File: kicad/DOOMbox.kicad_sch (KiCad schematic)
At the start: 1 part, among them U1 Pico

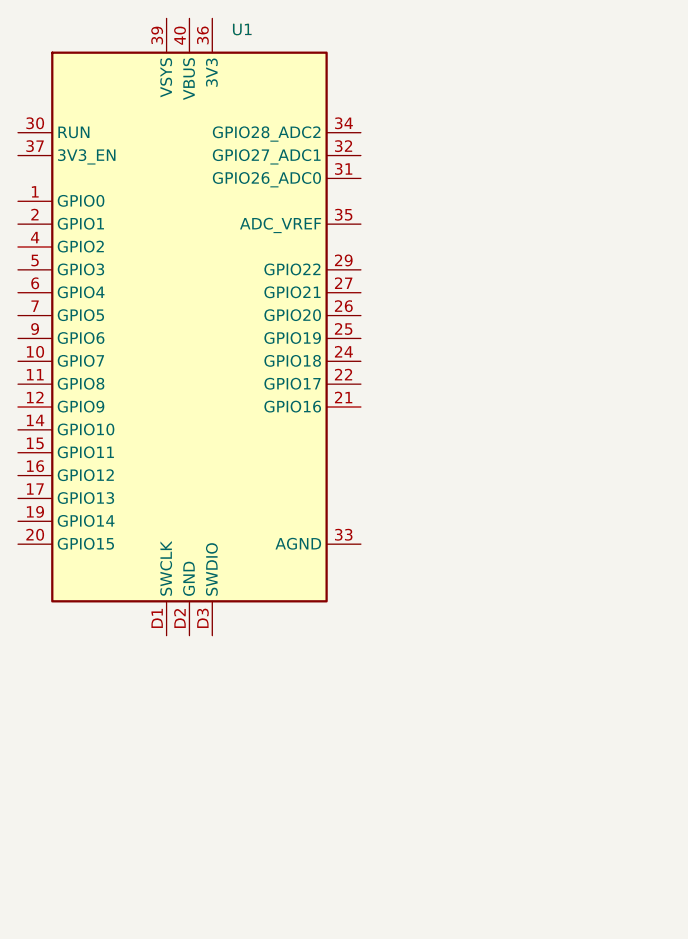
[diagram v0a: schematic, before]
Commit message: Track necessary KiCad libraries + symbols
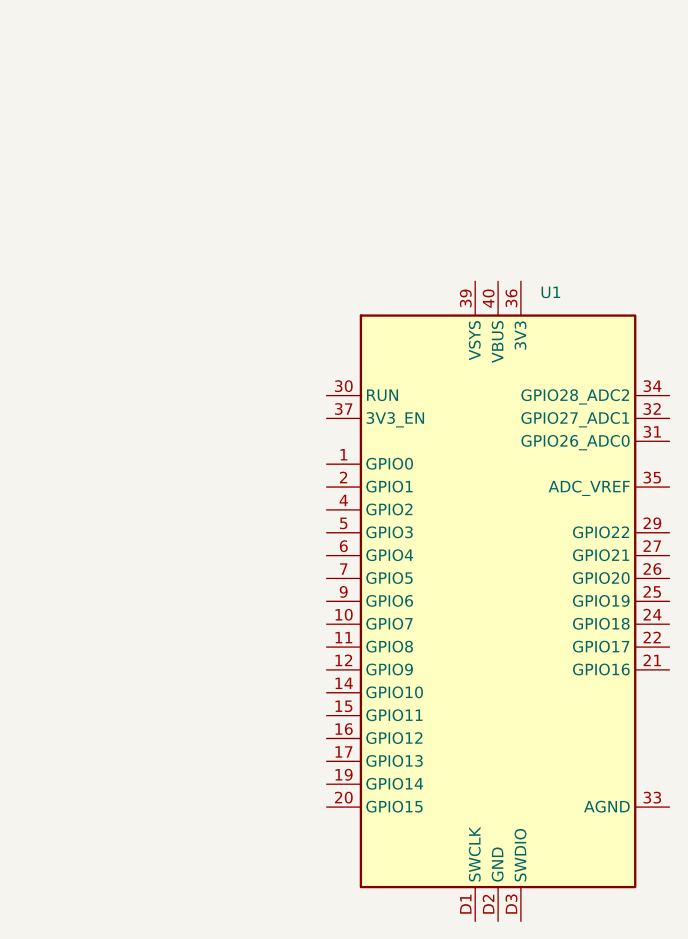
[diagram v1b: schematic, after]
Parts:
- removed U1: Pico, RPi_Pico:RPi_Pico_SMD_TH, symbol MCU_RaspberryPi_and_Boards:Pico
- added U1: RPi_Pico_SMD_TH, MCU_RPi:RPi_Pico_SMD_TH, symbol MCU_RPi:RPi_Pico_SMD_TH
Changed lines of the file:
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@@
 	(paper "A4")
 	(symbol
-		(lib_id "MCU_RaspberryPi_and_Boards:Pico")
-		(at 71.12 62.23 0)
+		(lib_id "MCU_RPi:RPi_Pico_SMD_TH")
+		(at 105.41 91.44 0)
 		(unit 1)
 		(exclude_from_sim no)
@@
 		(fields_autoplaced yes)
 		(property "Reference" "U1"
-			(at 75.8033 31.75 0)
+			(at 110.0933 60.96 0)
 			(effects
 				(font
@@
 			)
 		)
-		(property "Value" "Pico"
-			(at 71.12 72.898 0)
+		(property "Value" "RPi_Pico_SMD_TH"
+			(at 105.41 102.108 0)
 			(effects
 				(font
@@
 			)
 		)
-		(property "Footprint" "RPi_Pico:RPi_Pico_SMD_TH"
-			(at 70.612 70.358 0)
+		(property "Footprint" "MCU_RPi:RPi_Pico_SMD_TH"
+			(at 104.902 99.568 0)
 			(effects
 				(font
@@
 		)
 		(property "Datasheet" ""
-			(at 71.12 62.23 0)
+			(at 105.41 91.44 0)
 			(effects
 				(font
@@
 		)
 		(property "Description" ""
-			(at 71.12 62.23 0)
+			(at 105.41 91.44 0)
 			(effects
 				(font
@@
 			)
 		)
-		(pin "34"
+		(pin "D2"
+		)
+		(pin "D1"
+		)
+		(pin "33"
+		)
+		(pin "29"
+		)
+		(pin "19"
+		)
+		(pin "26"
+		)
+		(pin "35"
+		)
+		(pin "7"
+		)
+		(pin "16"
+		)
+		(pin "11"
+		)
+		(pin "D3"
+		)
+		(pin "25"
+		)
+		(pin "9"
+		)
+		(pin "21"
+		)
+		(pin "31"
+		)
+		(pin "22"
+		)
+		(pin "40"
+		)
+		(pin "24"
+		)
+		(pin "10"
+		)
+		(pin "27"
+		)
+		(pin "36"
+		)
+		(pin "20"
+		)
+		(pin "39"
+		)
+		(pin "17"
 		)
 		(pin "32"
 		)
-		(pin "36"
-		)
-		(pin "26"
-		)
-		(pin "D3"
-		)
-		(pin "14"
-		)
-		(pin "39"
+		(pin "34"
 		)
 		(pin "37"
@@
 		(pin "30"
 		)
+		(pin "1"
+		)
 		(pin "5"
 		)
-		(pin "22"
+		(pin "4"
 		)
-		(pin "D2"
+		(pin "2"
 		)
-		(pin "24"
+		(pin "12"
 		)
-		(pin "29"
-		)
-		(pin "7"
-		)
-		(pin "40"
-		)
-		(pin "35"
-		)
-		(pin "19"
+		(pin "14"
 		)
 		(pin "15"
 		)
-		(pin "9"
-		)
-		(pin "17"
-		)
-		(pin "4"
-		)
-		(pin "16"
-		)
-		(pin "25"
-		)
-		(pin "10"
-		)
-		(pin "D1"
-		)
 		(pin "6"
 		)
-		(pin "12"
-		)
-		(pin "31"
-		)
-		(pin "20"
-		)
-		(pin "33"
-		)
-		(pin "2"
-		)
-		(pin "21"
-		)
-		(pin "27"
-		)
-		(pin "11"
-		)
-		(pin "1"
-		)
 		(instances

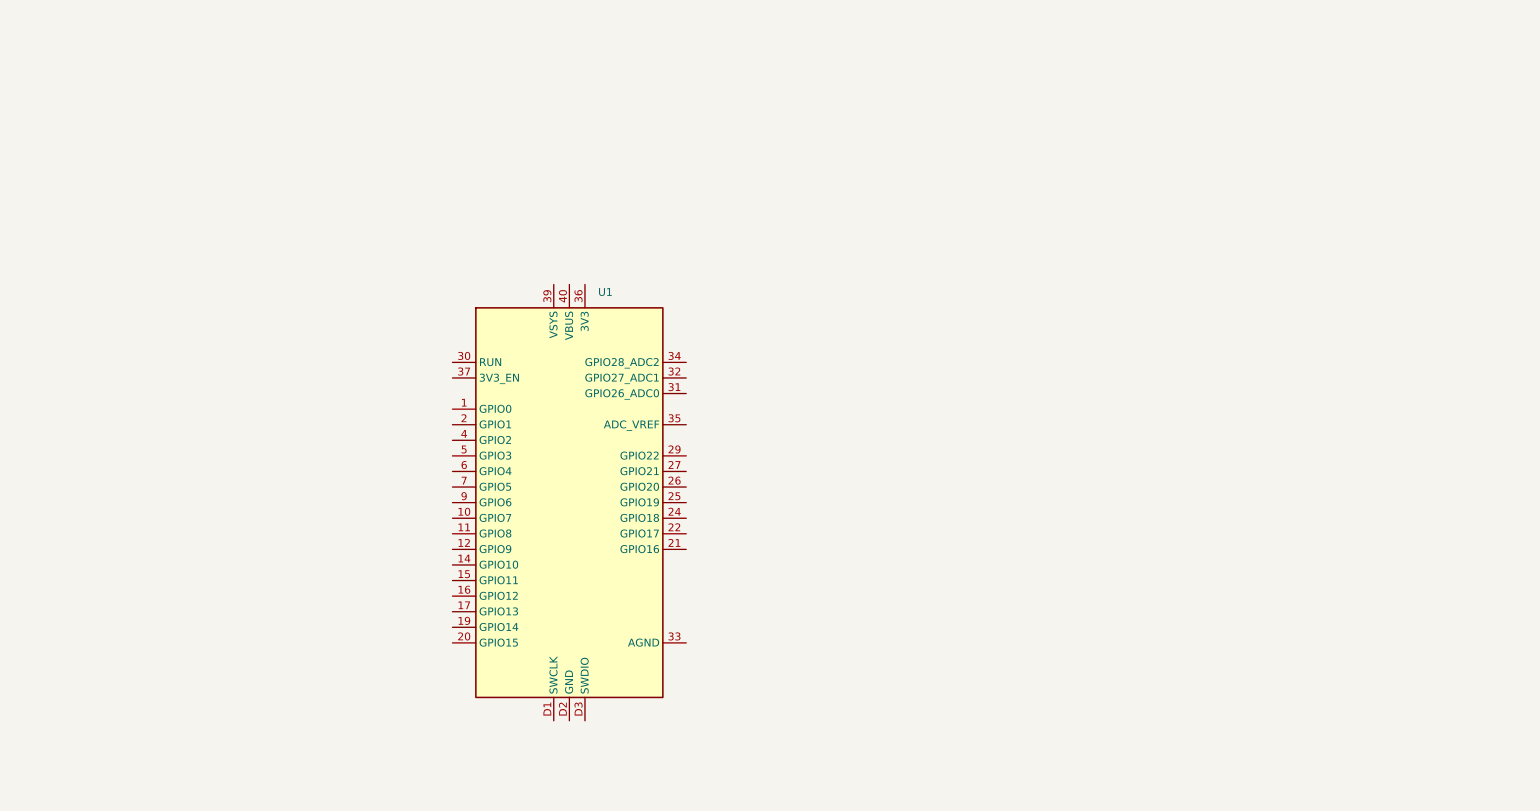
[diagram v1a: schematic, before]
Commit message: Schematic: add resistor ladder DACs for video data output
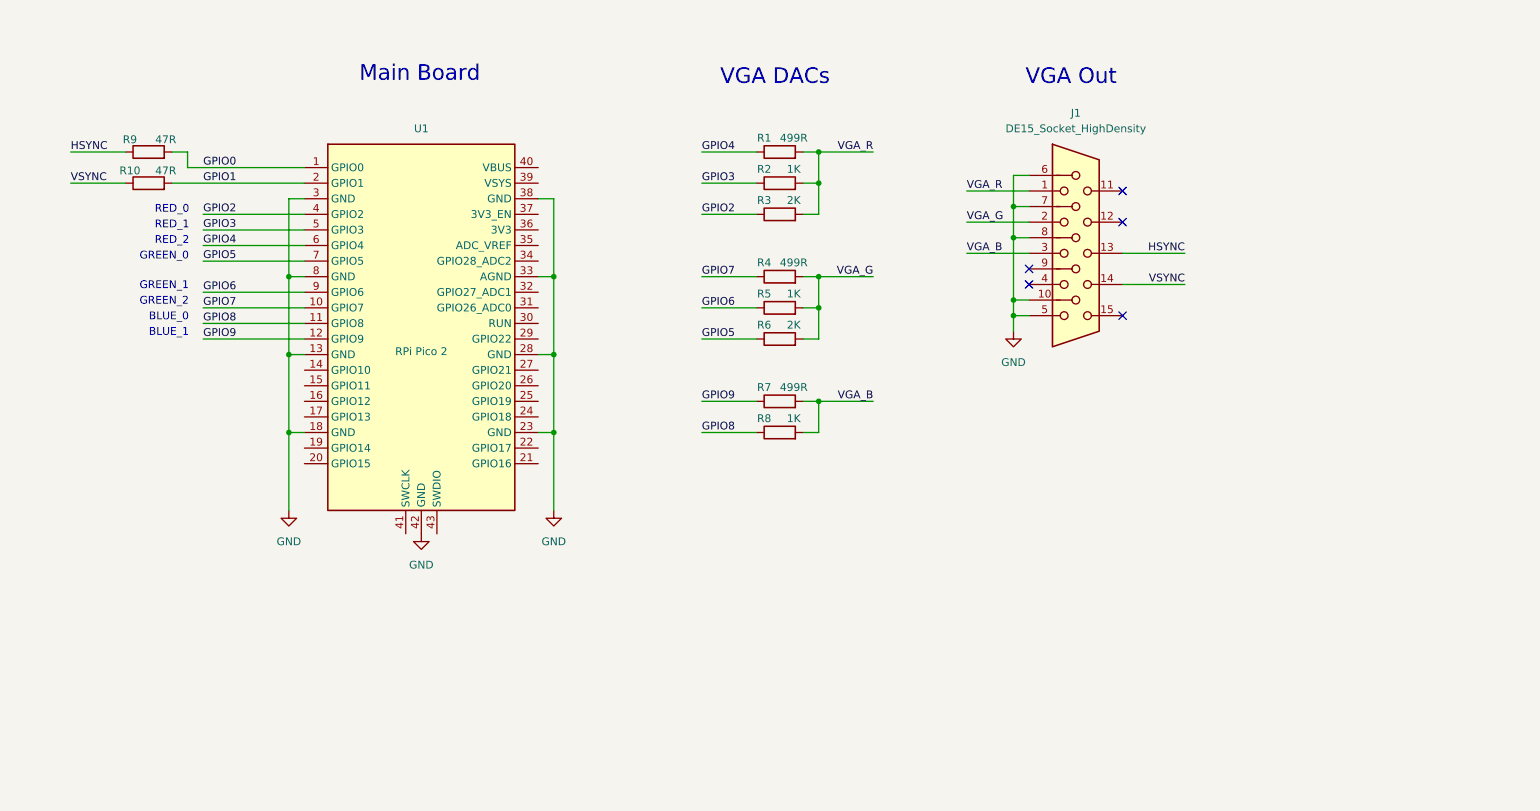
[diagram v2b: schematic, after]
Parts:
- added J1: DE15_Socket_HighDensity, symbol Connector:DE15_Socket_HighDensity
- added R1, R4, R7: 499R, symbol Device:R
- added R10, R9: 47R, symbol Device:R
- added R2, R5, R8: 1K, symbol Device:R
- added R3, R6: 2K, symbol Device:R
- U1: value RPi_Pico_SMD_TH -> RPi Pico 2
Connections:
- net GPIO0: now reaches U1.1 (GPIO0)
- net GPIO0: now also R9.2
- net GPIO7: now reaches U1.10 (GPIO7)
- net GPIO7: now also R4.1
- net GPIO8: now reaches U1.11 (GPIO8)
- net GPIO8: now also R8.1
- net GPIO9: now reaches U1.12 (GPIO9)
- net GPIO9: now also R7.1
- net GPIO1: now reaches U1.2 (GPIO1)
- net GPIO1: now also R10.2
- net GND: now reaches U1.33 (AGND)
- net GND: now also U1.13 (GND), U1.18 (GND), U1.23 (GND), U1.28 (GND), U1.3 (GND), U1.38 (GND), U1.42 (GND), U1.8 (GND), J1.10, J1.5, J1.6, J1.7, J1.8
- net GPIO2: now reaches U1.4 (GPIO2)
- net GPIO2: now also R3.1
- net GPIO3: now reaches U1.5 (GPIO3)
- net GPIO3: now also R2.1
- net GPIO4: now reaches U1.6 (GPIO4)
- net GPIO4: now also R1.1
- net GPIO5: now reaches U1.7 (GPIO5)
- net GPIO5: now also R6.1
- net GPIO6: now reaches U1.9 (GPIO6)
- net GPIO6: now also R5.1
- new net HSYNC: J1.13, R9.1
- new net VGA_B: J1.3, R7.2, R8.2
- new net VGA_G: J1.2, R4.2, R5.2, R6.2
- new net VGA_R: J1.1, R1.2, R2.2, R3.2
- new net VSYNC: J1.14, R10.1
- no-connect marks 0 -> 5
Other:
- note added: "BLUE_0"
- note added: "BLUE_1"
- note added: "GREEN_0"
- note added: "GREEN_1"
- note added: "GREEN_2"
- note added: "Main Board"
- note added: "RED_0"
- note added: "RED_1"
- note added: "RED_2"
- note added: "VGA DACs"
- note added: "VGA Out"

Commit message: Add component sheet + VGA output note in schematic
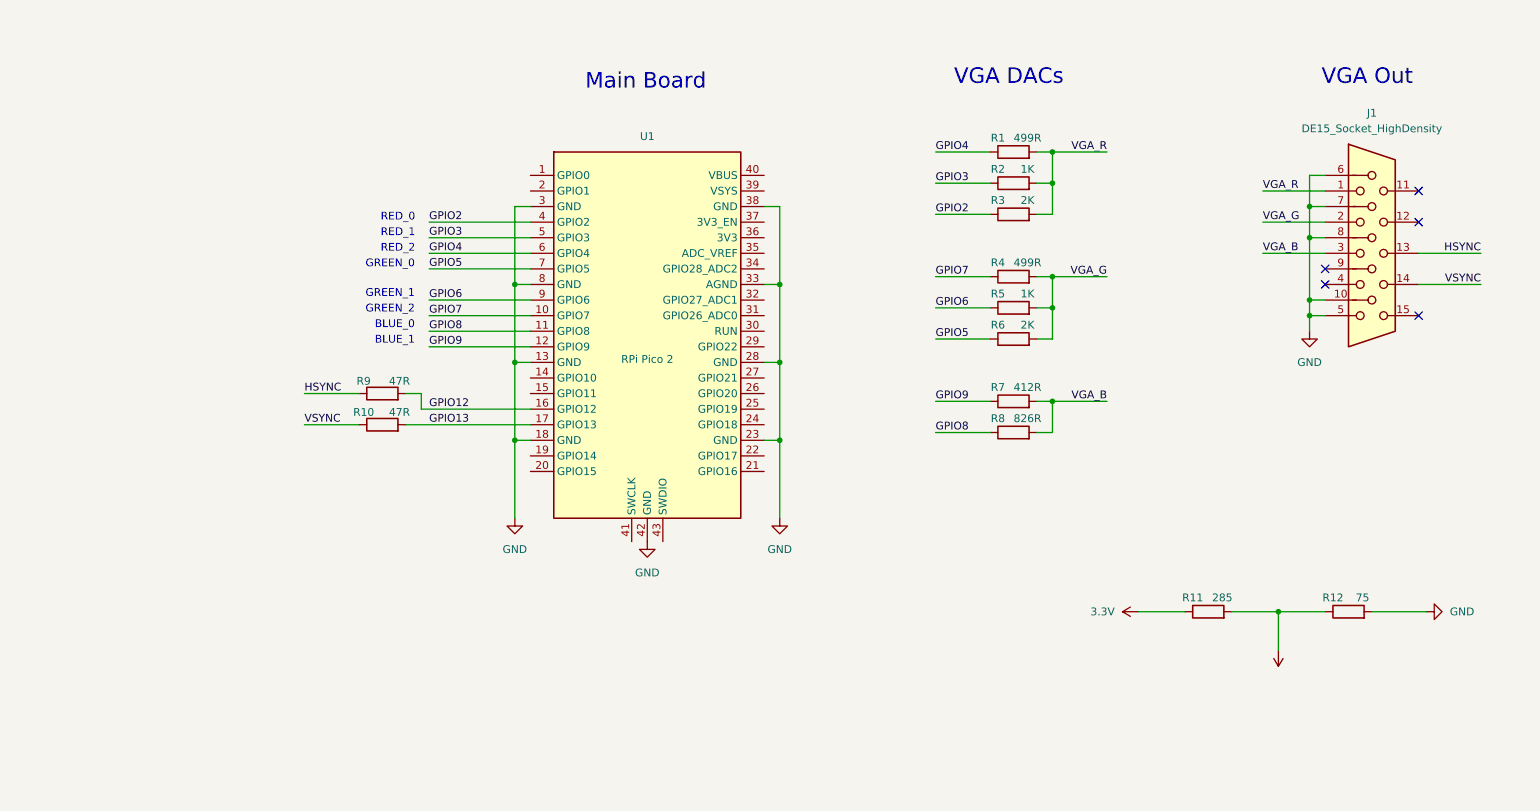
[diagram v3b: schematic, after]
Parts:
- added R11: 285, symbol Device:R
- added R12: 75, symbol Device:R
- R7: value 499R -> 412R
- R8: value 1K -> 826R
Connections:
- net GND: now also R12.2
- net GPIO12: now reaches U1.16 (GPIO12)
- net GPIO12: now also R9.2
- net GPIO13: now reaches U1.17 (GPIO13)
- net GPIO13: now also R10.2
- net GPIO0: no longer names the net of U1.1 (GPIO0)
- net GPIO0: no longer R9.2
- net GPIO1: no longer names the net of U1.2 (GPIO1)
- net GPIO1: no longer R10.2
- new net: R11.2, R12.1
- new net 3.3V: R11.1
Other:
- moved on the sheet: J1, R1, R10, R2, R3, R4, R5, R6, R7, R8, R9, U1

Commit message: Finalise VGA output schematic now w/ MCP23S08 SPI expander
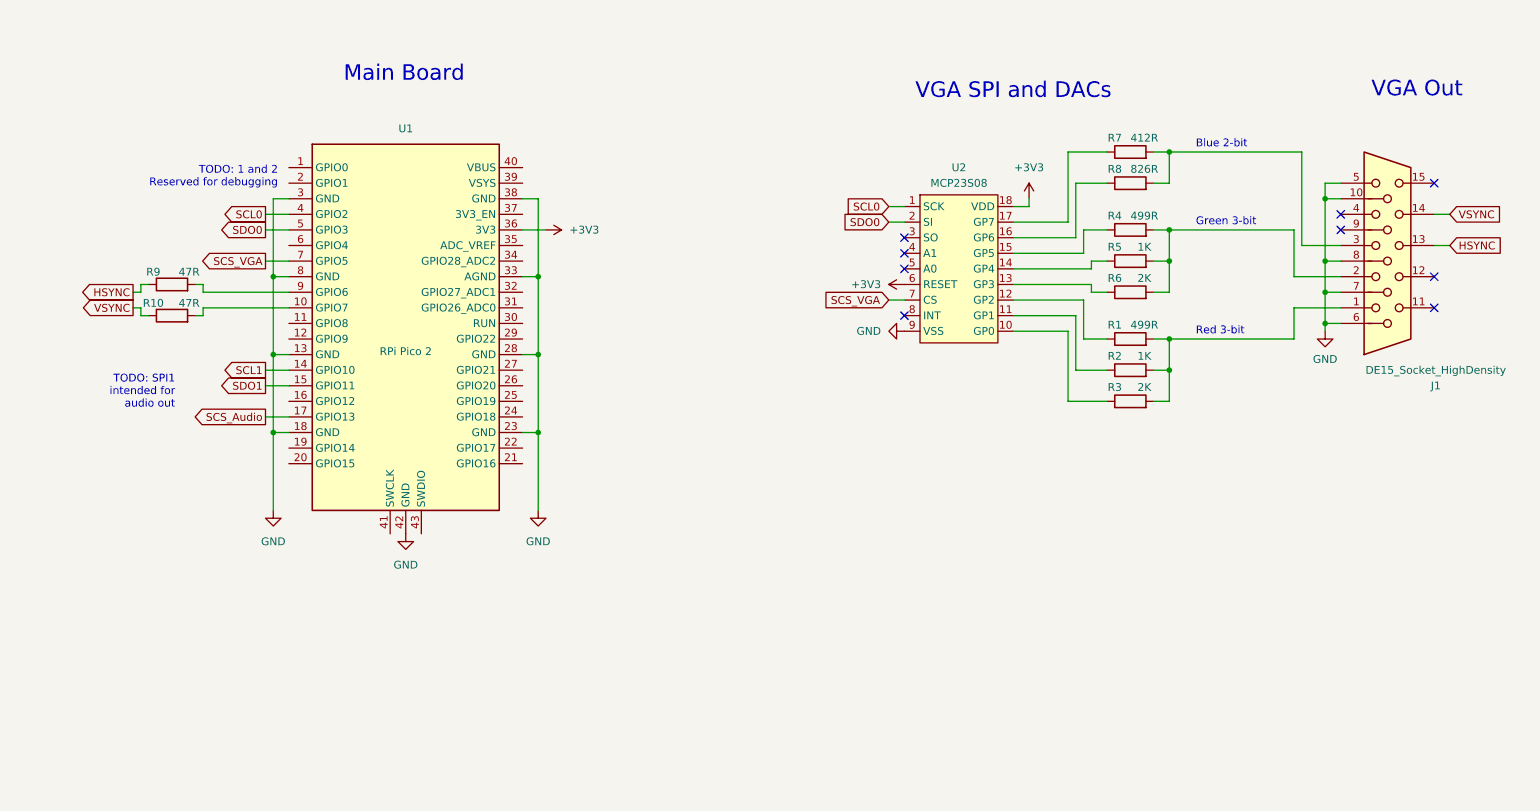
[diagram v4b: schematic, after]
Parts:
- removed R11: 285, symbol Device:R
- removed R12: 75, symbol Device:R
- added U2: MCP23S08, symbol Owen:MCP23S08
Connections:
- net GND: now also U2.9 (VSS)
- net SCL1: now reaches U1.14 (GPIO10)
- net SDO1: now reaches U1.15 (GPIO11)
- net +3V3: now reaches U1.36 (3V3)
- net +3V3: now also U2.18 (VDD), U2.6 (RESET)
- net GPIO12: no longer names the net of R9.2
- net GPIO12: now also U1.9 (GPIO6); no longer U1.16 (GPIO12)
- net GPIO13: no longer names the net of R10.2
- net GPIO13: now also U1.10 (GPIO7); no longer U1.17 (GPIO13)
- net GPIO2: no longer names the net of R3.1
- net GPIO2: now also U2.10 (GP0); no longer U1.4 (GPIO2)
- net GPIO3: no longer names the net of R2.1
- net GPIO3: now also U2.11 (GP1); no longer U1.5 (GPIO3)
- net GPIO4: no longer names the net of R1.1
- net GPIO4: now also U2.12 (GP2); no longer U1.6 (GPIO4)
- net GPIO5: no longer names the net of R6.1
- net GPIO5: now also U2.13 (GP3); no longer U1.7 (GPIO5)
- net GPIO6: no longer names the net of R5.1
- net GPIO6: now also U2.14 (GP4); no longer U1.9 (GPIO6)
- net GPIO7: no longer names the net of R4.1
- net GPIO7: now also U2.15 (GP5); no longer U1.10 (GPIO7)
- net GPIO8: no longer names the net of U1.11 (GPIO8)
- net GPIO8: no longer R8.1
- net GPIO9: no longer names the net of R7.1
- net GPIO9: now also U2.17 (GP7); no longer U1.12 (GPIO9)
- net VGA_B: no longer names the net of J1.3, R7.2, R8.2
- net VGA_G: no longer names the net of J1.2, R4.2, R5.2, R6.2
- net VGA_R: no longer names the net of J1.1, R1.2, R2.2, R3.2
- new net: R8.1, U2.16 (GP6)
- new net SCL0: U1.4 (GPIO2), U2.1 (SCK)
- new net SCS_Audio: U1.17 (GPIO13)
- new net SCS_VGA: U1.7 (GPIO5), U2.7 (CS)
- new net SDO0: U1.5 (GPIO3), U2.2 (SI)
- no-connect marks 5 -> 9
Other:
- note added: "Blue 2-bit"
- note added: "Green 3-bit"
- note added: "Red 3-bit"
- note added: "TODO: 1 and 2 Reserved for debugging"
- note added: "TODO: SPI1 intended for audio out"
- note added: "VGA SPI and DACs"
- note removed: "BLUE_0"
- note removed: "BLUE_1"
- note removed: "GREEN_0"
- note removed: "GREEN_1"
- note removed: "GREEN_2"
- note removed: "RED_0"
- note removed: "RED_1"
- note removed: "RED_2"
- note removed: "VGA DACs"
- moved on the sheet: R1, R10, R2, R3, R4, R5, R6, R7, R8, R9, U1

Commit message: More schematic changes
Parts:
- removed U2: MCP23S08, symbol Owen:MCP23S08
- added U2: MCP23S08, symbol MCU_Microchip_MCP:MCP23S08
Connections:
- net +3V3: now also U2.18 (VDD), U2.6 (~{RESET})
- net GND: now also U2.9 (VSS)
- net SCL0: now also U2.1 (SCK)
- net SCS_VGA: now also U2.7 (~{CS})
- net SDO0: now also U2.2 (SI)
- net at R3.1: now also U2.10 (GP0)
- net at R2.1: now also U2.11 (GP1)
- net at R1.1: now also U2.12 (GP2)
- net at R7.1: now also U2.17 (GP7)
- net at R5.1: now also U2.14 (GP4)
- net at R8.1: now also U2.16 (GP6)
- net at R4.1: now also U2.15 (GP5)
- net at R6.1: now also U2.13 (GP3)
- no-connect marks 9 -> 10
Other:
- moved on the sheet: J1, R1, R2, R3, R4, R5, R6, R7, R8
